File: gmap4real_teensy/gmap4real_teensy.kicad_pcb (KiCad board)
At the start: 2 copper layers, 149.9 x 54.6 mm, 25 parts

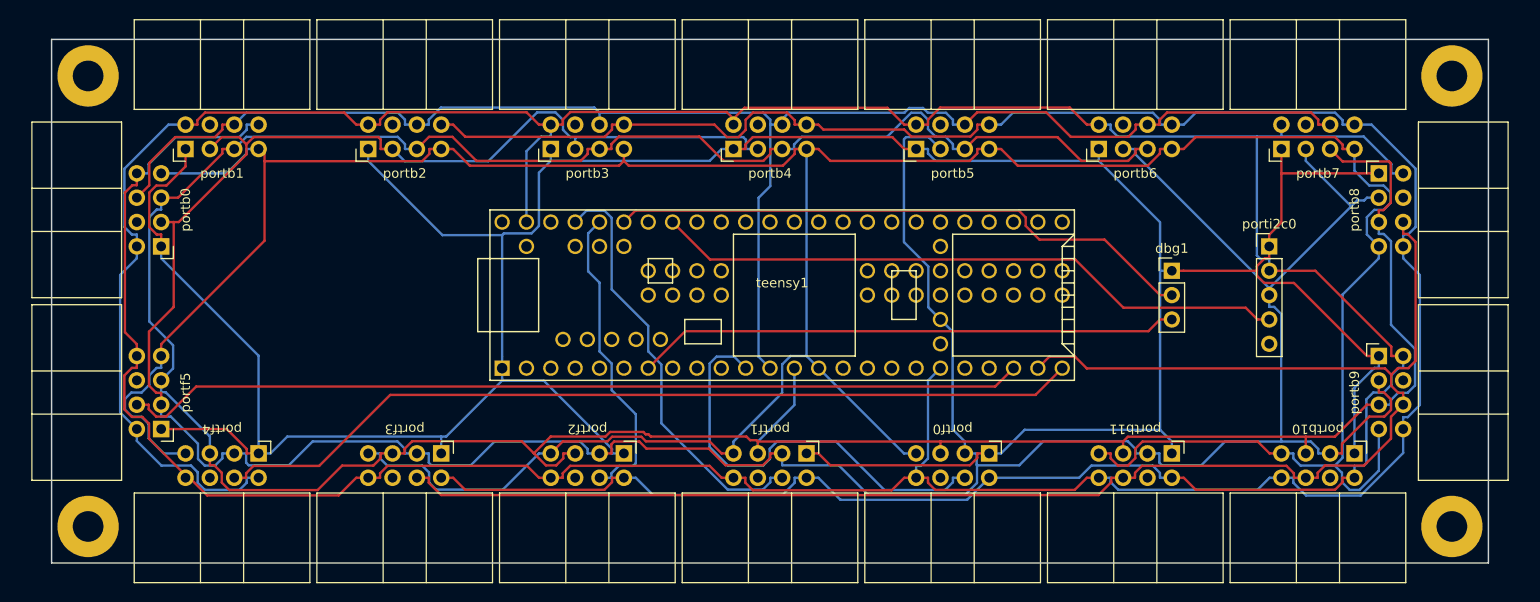
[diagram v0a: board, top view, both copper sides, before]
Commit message: smaller PCBs
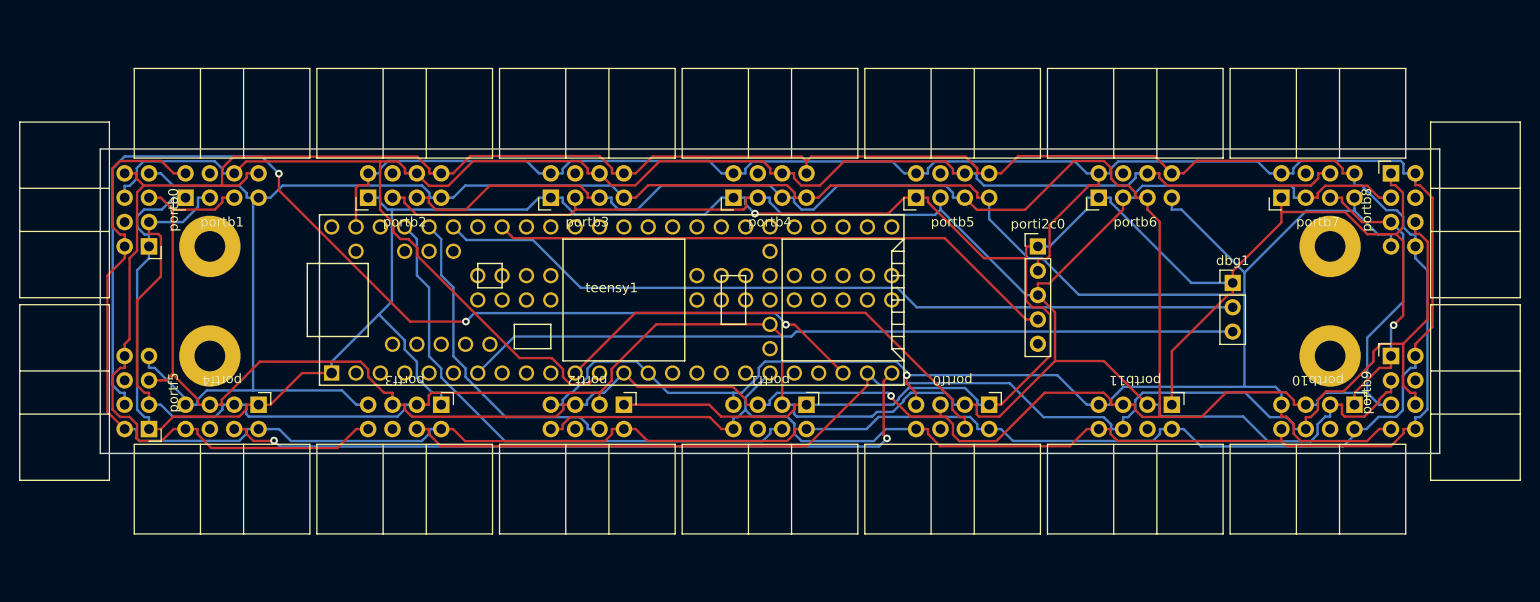
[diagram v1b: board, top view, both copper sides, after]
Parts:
- moved porti2c0 24.1 mm to (170.2, 88.9)
- moved hole2 21.8 mm to (200.7, 88.9)
- moved hole4 21.8 mm to (200.7, 100.3)
- moved hole1 21.8 mm to (83.8, 88.9)
- moved hole3 21.8 mm to (83.8, 100.3)
- moved teensy1 17.8 mm to (125.7, 94.5)
- moved dbg1 6.48 mm to (190.5, 92.7)
- moved portb1 5.08 mm to (81.3, 83.8)
- moved portb10 5.08 mm to (203.2, 105.4)
- moved portb11 5.08 mm to (184.2, 105.4)
- moved portb2 5.08 mm to (100.3, 83.8)
- moved portb3 5.08 mm to (119.4, 83.8)
- moved portb4 5.08 mm to (138.4, 83.8)
- moved portb5 5.08 mm to (157.5, 83.8)
- moved portb6 5.08 mm to (176.5, 83.8)
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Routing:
- net 3.3v: track 361.8 -> 323.6 mm
- net cs05: track 172.0 -> 142.8 mm
- net miso0: track 351.9 -> 325.5 mm, vias 0 -> 1
- net dbgtx: track 56.7 -> 80.5 mm
- net dbgrx: track 61.8 -> 84.8 mm
- net gnd: track 339.5 -> 319.3 mm, vias 0 -> 2
- net mosi0: track 339.9 -> 320.6 mm, vias 0 -> 1
- net cs07: track 94.3 -> 113.3 mm, vias 0 -> 3
- net cs06: track 91.4 -> 76.8 mm, vias 0 -> 2
- net cs00: track 166.7 -> 179.0 mm
- net cs02: track 44.4 -> 56.4 mm
- net agnd: track 358.2 -> 348.4 mm
- net sck0: track 348.0 -> 338.9 mm
- net i2cscl0: track 66.4 -> 59.9 mm
- net cs01: track 45.2 -> 49.6 mm
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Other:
- board size 149.9 x 54.6 mm -> 139.7 x 31.8 mm

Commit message: teensy: fix select pin conflict
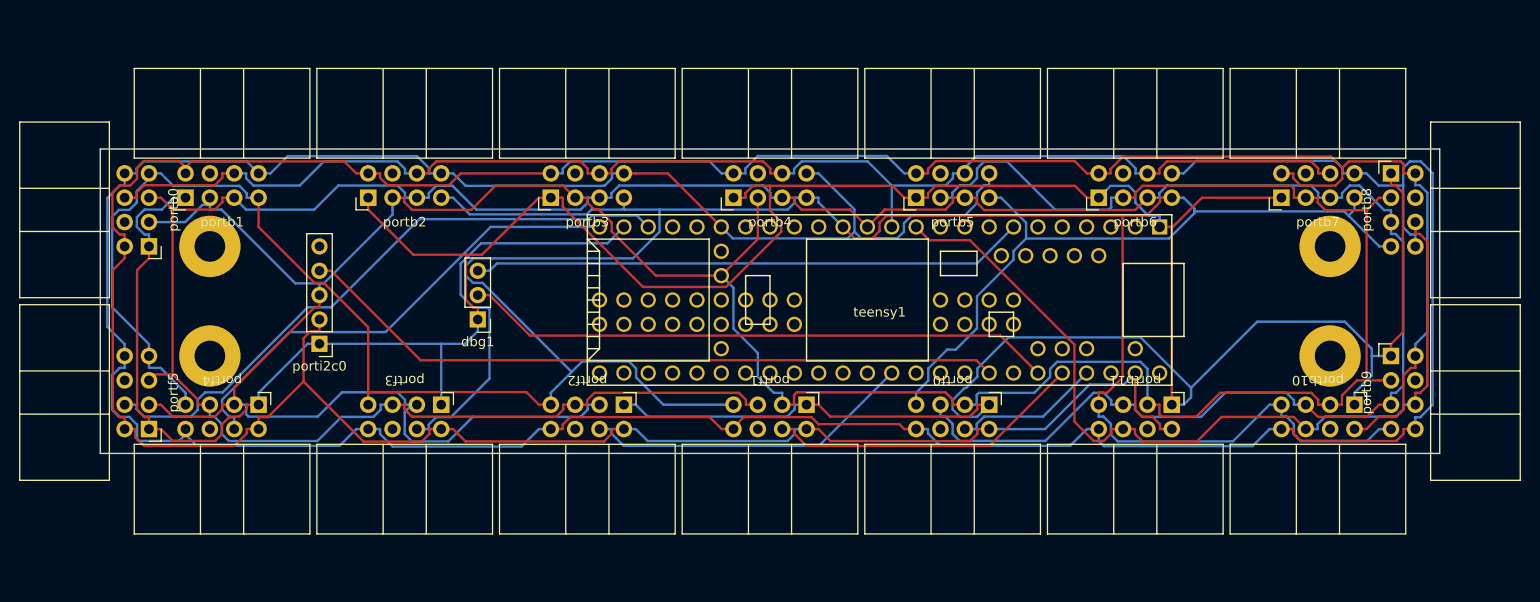
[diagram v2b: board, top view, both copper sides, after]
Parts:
- moved dbg1 78.8 mm to (111.8, 96.5), turned to 180 degrees
- moved porti2c0 75.6 mm to (95.2, 99.1), turned to 180 degrees
- moved teensy1 27.9 mm to (153.7, 94.5), turned to 180 degrees
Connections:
- portb0 pad 4: (no net) -> Net-(portb0-Pad4)
- portb1 pad 4: (no net) -> Net-(portb1-Pad4)
- portb10 pad 4: (no net) -> Net-(portb10-Pad4)
- portb10 pad 6: cs05 -> cs01
- portb11 pad 4: (no net) -> Net-(portb11-Pad4)
- portb11 pad 6: cs05 -> cs01
- portb2 pad 4: (no net) -> Net-(portb2-Pad4)
- portb3 pad 4: (no net) -> Net-(portb3-Pad4)
- portb4 pad 4: (no net) -> Net-(portb4-Pad4)
- portb5 pad 4: (no net) -> Net-(portb5-Pad4)
- portb6 pad 4: (no net) -> Net-(portb6-Pad4)
- portb7 pad 4: (no net) -> Net-(portb7-Pad4)
- portb8 pad 4: (no net) -> Net-(portb8-Pad4)
- portb8 pad 6: cs05 -> cs01
- portb9 pad 4: (no net) -> Net-(portb9-Pad4)
- portb9 pad 6: cs05 -> cs01
- portf0 pad 4: cs01 -> cs02
- portf0 pad 6: (no net) -> Net-(portf0-Pad6)
- portf1 pad 4: cs02 -> cs03
- portf1 pad 6: (no net) -> Net-(portf1-Pad6)
- portf2 pad 4: cs03 -> cs04
- portf2 pad 6: (no net) -> Net-(portf2-Pad6)
- portf3 pad 6: (no net) -> Net-(portf3-Pad6)
- portf4 pad 6: (no net) -> Net-(portf4-Pad6)
- portf5 pad 6: (no net) -> Net-(portf5-Pad6)
- porti2c0 pad 5: (no net) -> i2csda0
- teensy1 pad 10: (no net) -> Net-(teensy1-Pad10)
- teensy1 pad 15: (no net) -> Net-(teensy1-Pad15)
- teensy1 pad 16: (no net) -> Net-(teensy1-Pad16)
- teensy1 pad 17: (no net) -> Net-(teensy1-Pad17)
- teensy1 pad 18: (no net) -> Net-(teensy1-Pad18)
- teensy1 pad 2: (no net) -> Net-(teensy1-Pad2)
- teensy1 pad 20: (no net) -> Net-(teensy1-Pad20)
- teensy1 pad 21: (no net) -> Net-(teensy1-Pad21)
- teensy1 pad 25: (no net) -> Net-(teensy1-Pad25)
- teensy1 pad 27: (no net) -> Net-(teensy1-Pad27)
- teensy1 pad 28: (no net) -> Net-(teensy1-Pad28)
- teensy1 pad 29: (no net) -> Net-(teensy1-Pad29)
- teensy1 pad 3: (no net) -> Net-(teensy1-Pad3)
- teensy1 pad 30: (no net) -> Net-(teensy1-Pad30)
- teensy1 pad 31: (no net) -> Net-(teensy1-Pad31)
- teensy1 pad 32: (no net) -> Net-(teensy1-Pad32)
- teensy1 pad 33: (no net) -> Net-(teensy1-Pad33)
- teensy1 pad 34: (no net) -> Net-(teensy1-Pad34)
- teensy1 pad 35: (no net) -> Net-(teensy1-Pad35)
- teensy1 pad 36: (no net) -> Net-(teensy1-Pad36)
- teensy1 pad 37: (no net) -> Net-(teensy1-Pad37)
- teensy1 pad 38: (no net) -> Net-(teensy1-Pad38)
- teensy1 pad 39: (no net) -> Net-(teensy1-Pad39)
- teensy1 pad 4: (no net) -> Net-(teensy1-Pad4)
- teensy1 pad 40: (no net) -> Net-(teensy1-Pad40)
- teensy1 pad 41: (no net) -> Net-(teensy1-Pad41)
- teensy1 pad 42: (no net) -> cs04
- teensy1 pad 43: (no net) -> Net-(teensy1-Pad43)
- teensy1 pad 44: (no net) -> Net-(teensy1-Pad44)
- teensy1 pad 45: (no net) -> i2csca0
- teensy1 pad 47: (no net) -> Net-(teensy1-Pad47)
- teensy1 pad 5: (no net) -> Net-(teensy1-Pad5)
- teensy1 pad 51: (no net) -> Net-(teensy1-Pad51)
- teensy1 pad 53: (no net) -> Net-(teensy1-Pad53)
- teensy1 pad 54: (no net) -> Net-(teensy1-Pad54)
- teensy1 pad 55: (no net) -> Net-(teensy1-Pad55)
- teensy1 pad 56: (no net) -> Net-(teensy1-Pad56)
- teensy1 pad 57: (no net) -> Net-(teensy1-Pad57)
- teensy1 pad 58: (no net) -> Net-(teensy1-Pad58)
- teensy1 pad 59: (no net) -> Net-(teensy1-Pad59)
- teensy1 pad 6: (no net) -> Net-(teensy1-Pad6)
- teensy1 pad 60: (no net) -> Net-(teensy1-Pad60)
- teensy1 pad 61: (no net) -> Net-(teensy1-Pad61)
- teensy1 pad 62: (no net) -> Net-(teensy1-Pad62)
- teensy1 pad 63: (no net) -> Net-(teensy1-Pad63)
- teensy1 pad 64: (no net) -> Net-(teensy1-Pad64)
- teensy1 pad 65: (no net) -> Net-(teensy1-Pad65)
- teensy1 pad 66: (no net) -> Net-(teensy1-Pad66)
- teensy1 pad 67: (no net) -> Net-(teensy1-Pad67)
- teensy1 pad 68: (no net) -> Net-(teensy1-Pad68)
- teensy1 pad 69: (no net) -> Net-(teensy1-Pad69)
- teensy1 pad 70: (no net) -> Net-(teensy1-Pad70)
- teensy1 pad 71: (no net) -> Net-(teensy1-Pad71)
- teensy1 pad 72: (no net) -> Net-(teensy1-Pad72)
- teensy1 pad 73: (no net) -> Net-(teensy1-Pad73)
- teensy1 pad 74: (no net) -> Net-(teensy1-Pad74)
- teensy1 pad 75: (no net) -> Net-(teensy1-Pad75)
- teensy1 pad 76: (no net) -> Net-(teensy1-Pad76)
- teensy1 pad 77: (no net) -> Net-(teensy1-Pad77)
- teensy1 pad 78: (no net) -> Net-(teensy1-Pad78)
- teensy1 pad 79: (no net) -> Net-(teensy1-Pad79)
- teensy1 pad 8: (no net) -> Net-(teensy1-Pad8)
- teensy1 pad 80: (no net) -> Net-(teensy1-Pad80)
- teensy1 pad 81: (no net) -> Net-(teensy1-Pad81)
- teensy1 pad 82: (no net) -> Net-(teensy1-Pad82)
- teensy1 pad 83: (no net) -> Net-(teensy1-Pad83)
- teensy1 pad 84: (no net) -> Net-(teensy1-Pad84)
- teensy1 pad 85: (no net) -> Net-(teensy1-Pad85)
- teensy1 pad 86: (no net) -> Net-(teensy1-Pad86)
- teensy1 pad 9: (no net) -> Net-(teensy1-Pad9)
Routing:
- net cs05: track 142.8 -> 42.7 mm
- net cs07: track 113.3 -> 65.2 mm, vias 3 -> 0
- net miso0: track 325.5 -> 372.7 mm, vias 1 -> 0
- net gnd: track 319.3 -> 362.0 mm, vias 2 -> 0
- net cs01: track 49.6 -> 91.5 mm
- net cs02: track 56.4 -> 15.4 mm
- net cs00: track 179.0 -> 144.2 mm
- net cs04: track 0.00 -> 34.6 mm
- net cs06: track 76.8 -> 50.7 mm, vias 2 -> 0
- net dbgrx: track 84.8 -> 61.8 mm
- net dbgtx: track 80.5 -> 57.8 mm
- net sck0: track 338.9 -> 355.6 mm
- net i2cscl0: track 59.9 -> 74.3 mm
- net mosi0: track 320.6 -> 314.7 mm, vias 1 -> 0
- net agnd: track 348.4 -> 353.0 mm
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
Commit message: teensy: simplify (no agnd to buttons, no agnd to i2c port)
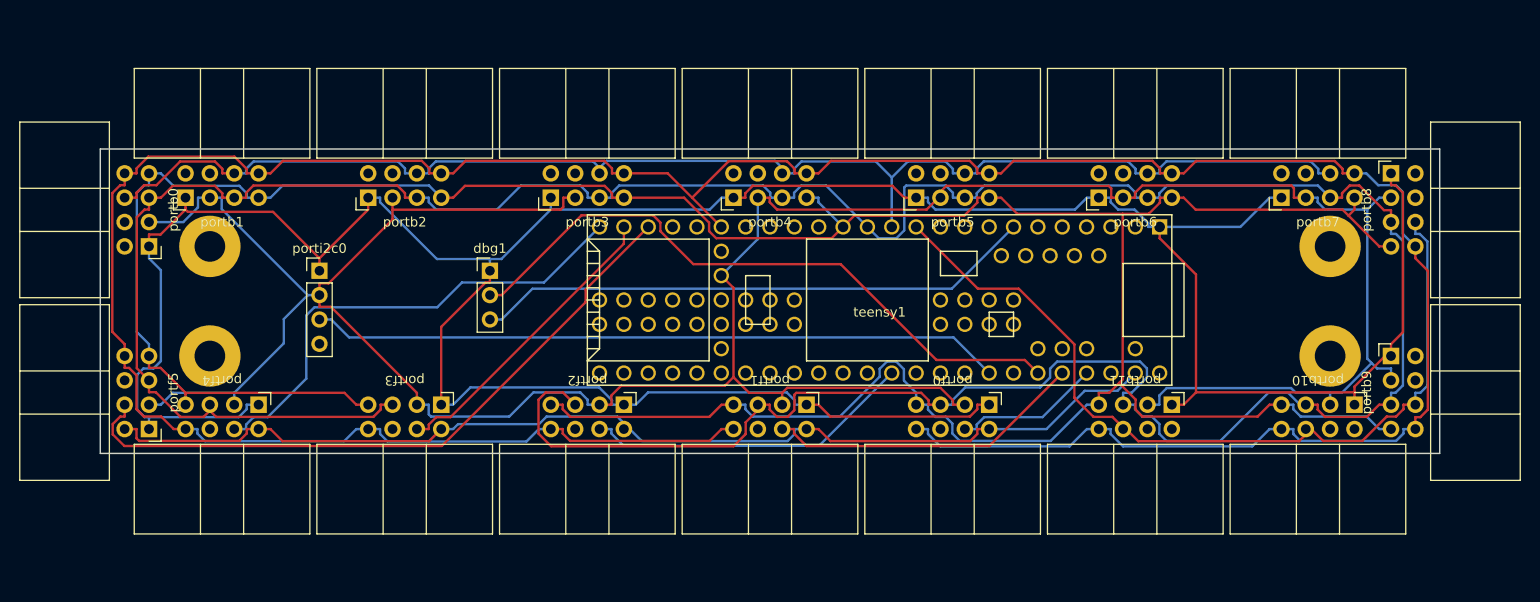
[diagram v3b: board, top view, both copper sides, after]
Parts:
- porti2c0: value Conn_01x05 -> Conn_01x04; footprint Connector_PinHeader_2.54mm:PinHeader_1x05_P2.54mm_Vertical -> Connector_PinHeader_2.54mm:PinHeader_1x04_P2.54mm_Vertical
- moved porti2c0 7.62 mm to (95.2, 91.4), turned to 0 degrees
- moved dbg1 5.24 mm to (113.0, 91.4), turned to 0 degrees
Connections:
- portb0 pad 2: agnd -> Net-(portb0-Pad2)
- portb1 pad 2: agnd -> Net-(portb1-Pad2)
- portb10 pad 2: agnd -> Net-(portb10-Pad2)
- portb11 pad 2: agnd -> Net-(portb11-Pad2)
- portb2 pad 2: agnd -> Net-(portb2-Pad2)
- portb3 pad 2: agnd -> Net-(portb3-Pad2)
- portb4 pad 2: agnd -> Net-(portb4-Pad2)
- portb5 pad 2: agnd -> Net-(portb5-Pad2)
- portb6 pad 2: agnd -> Net-(portb6-Pad2)
- portb7 pad 2: agnd -> Net-(portb7-Pad2)
- portb8 pad 2: agnd -> Net-(portb8-Pad2)
- portb9 pad 2: agnd -> Net-(portb9-Pad2)
- porti2c0 pad 2: agnd -> 3.3v
- porti2c0 pad 3: 3.3v -> i2cscl0
- porti2c0 pad 4: i2cscl0 -> i2csda0
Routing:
- net agnd: track 353.0 -> 115.1 mm
- net miso0: track 372.7 -> 319.4 mm
- net gnd: track 362.0 -> 320.2 mm
- net mosi0: track 314.7 -> 343.9 mm
- net sck0: track 355.6 -> 328.5 mm
- net 3.3v: track 327.8 -> 304.7 mm
- net cs05: track 42.7 -> 31.6 mm
- net dbgrx: track 61.8 -> 67.9 mm
- net cs07: track 65.2 -> 70.5 mm
- net cs01: track 91.5 -> 88.9 mm
- net i2cscl0: track 74.3 -> 72.2 mm
- net dbgtx: track 57.8 -> 58.6 mm
